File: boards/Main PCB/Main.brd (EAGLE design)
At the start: 101.6 x 76.2 mm, 89 parts, among them CN1 MINIB, CN2 MINIB, IC1 FT232RL, IC2 FT232RL, J1 3_PIN_JST-XH, J2 2_PIN_JST-XH, Q4 BSS138, Q5 BSS138, Q6 BSS138, Q7 BSS138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

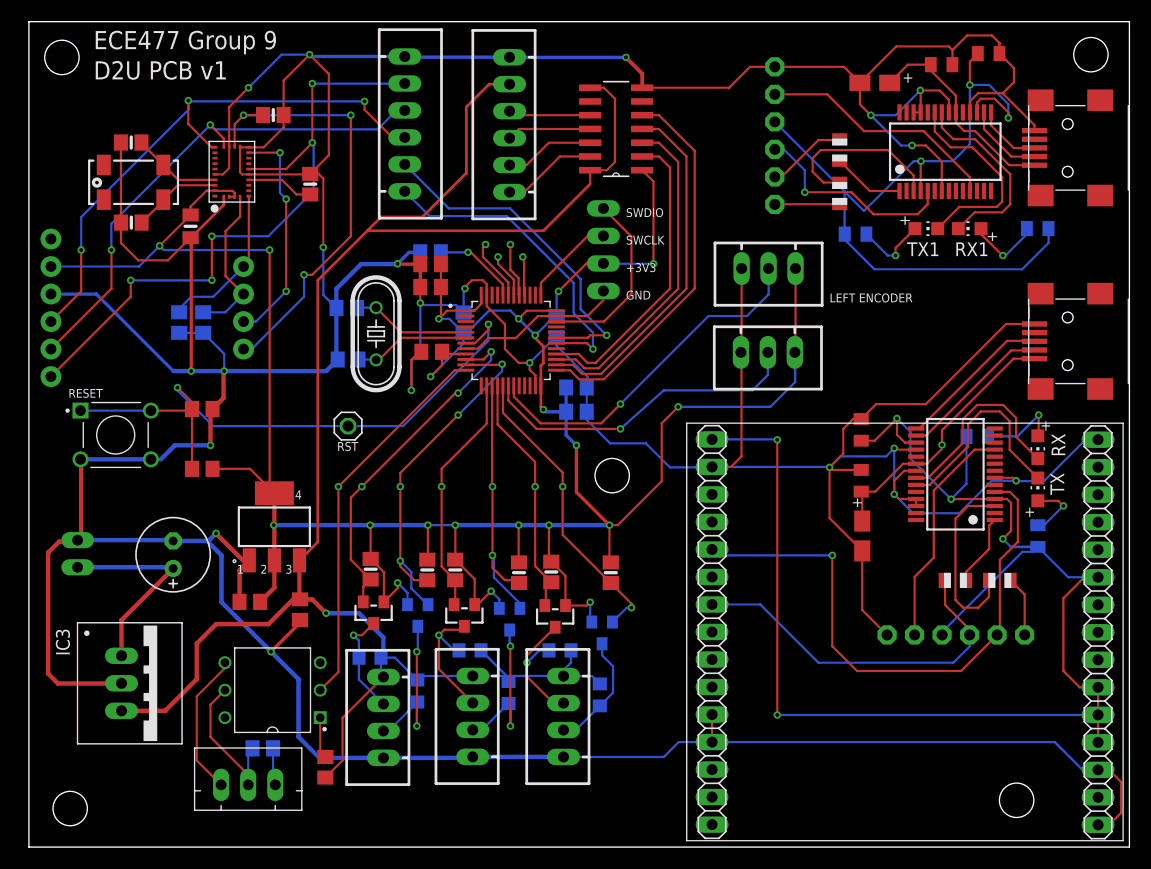
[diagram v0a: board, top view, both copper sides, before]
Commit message: Fixed minor routing problems
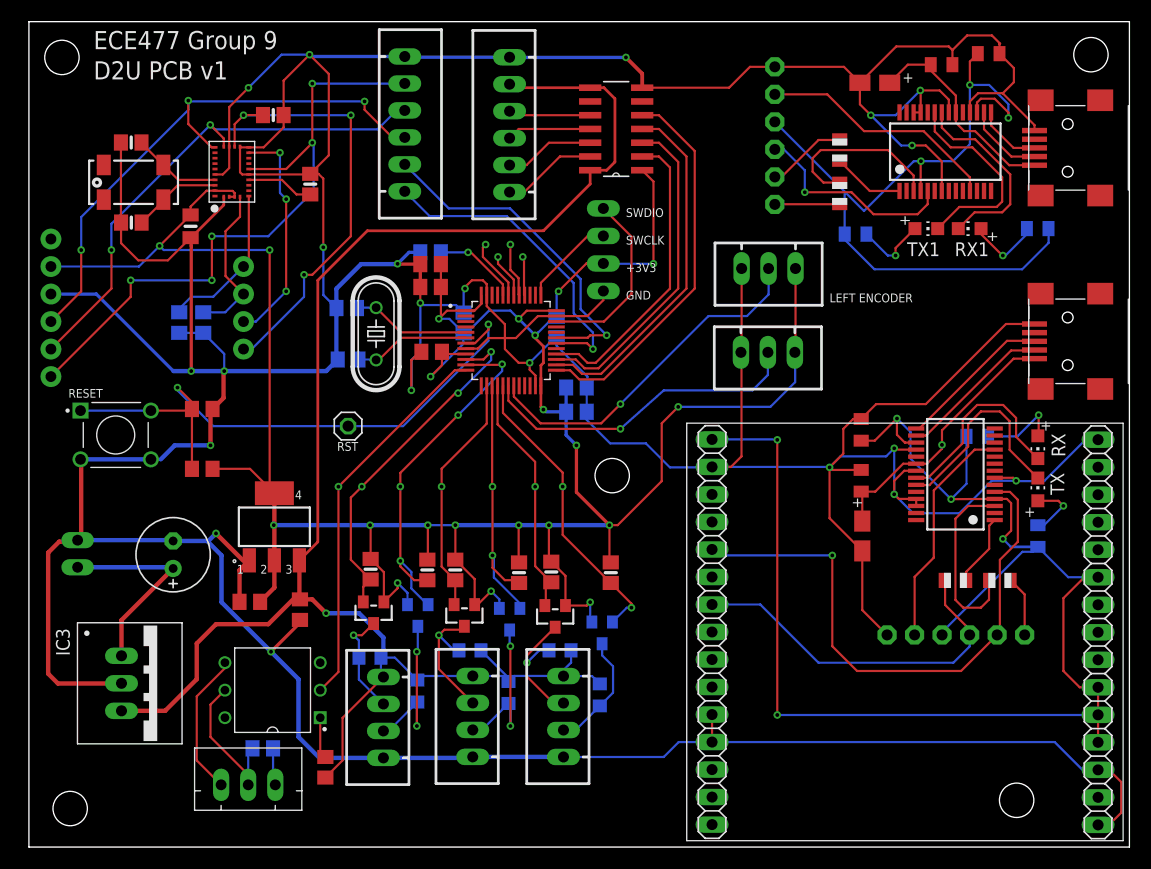
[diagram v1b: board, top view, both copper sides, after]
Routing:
- net +5V: track 169.6 -> 154.9 mm
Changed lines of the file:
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@@
 <?xml version="1.0" encoding="utf-8"?>
 <!DOCTYPE eagle SYSTEM "eagle.dtd">
-<eagle version="9.2.2">
+<eagle version="9.3.0">
 <drawing>
 <settings>
@@
 </element>
 <element name="C1" library="adafruit" package="A/3216-18R" value="10uF" x="76.936" y="28.716" smashed="yes" rot="R90">
-<attribute name="VALUE" x="79.261" y="26.766" size="0.6096" layer="27" rot="R90"/>
+<attribute name="VALUE" x="79.007" y="26.766" size="0.6096" layer="27" rot="R90"/>
 </element>
 <element name="C2" library="adafruit" package="C0805K" value="0.1uF" x="76.836" y="33.816" smashed="yes" rot="R90">
@@
 </element>
 <element name="R5" library="adafruit" package="R0805" value="10" x="85.536" y="24.616" smashed="yes">
-<attribute name="VALUE" x="84.774" y="22.33" size="0.6096" layer="27"/>
+<attribute name="VALUE" x="83.25" y="22.838" size="0.6096" layer="27"/>
 </element>
 <element name="FTDI" library="adafruit" package="1X06-CLEANBIG" value="" x="85.576" y="19.586" smashed="yes">
@@
 </element>
 <element name="R1" library="adafruit" package="R0805" value="10" x="89.636" y="24.616" smashed="yes" rot="R180">
-<attribute name="VALUE" x="90.398" y="26.902" size="0.6096" layer="27" rot="R180"/>
+<attribute name="VALUE" x="89.128" y="26.394" size="0.6096" layer="27" rot="R180"/>
 </element>
 <element name="U$3" library="microbuilder" package="BNO055" value="BNO055" x="18.74" y="62.346" smashed="yes" rot="R90">
@@
 <wire x1="26.67" y1="52.324" x2="31.242" y2="56.896" width="0.254" layer="1"/>
 <contactref element="X1" pad="5"/>
-<wire x1="31.242" y1="56.896" x2="32.512" y2="58.166" width="0.254" layer="1"/>
-<wire x1="32.512" y1="58.166" x2="36.322" y2="58.166" width="0.254" layer="1"/>
-<wire x1="36.322" y1="58.166" x2="40.386" y2="62.23" width="0.254" layer="1"/>
-<wire x1="40.386" y1="62.23" x2="40.386" y2="68.326" width="0.254" layer="1"/>
-<wire x1="40.386" y1="68.326" x2="42.4858" y2="70.4258" width="0.254" layer="1"/>
-<wire x1="42.4858" y1="70.4258" x2="44.374" y2="70.4258" width="0.254" layer="1"/>
 <contactref element="U4" pad="14"/>
 <contactref element="U4" pad="8"/>
-<wire x1="51.816" y1="70.104" x2="53.086" y2="70.104" width="0.2032" layer="1"/>
-<wire x1="53.086" y1="70.104" x2="54.102" y2="69.088" width="0.2032" layer="1"/>
-<wire x1="54.102" y1="69.088" x2="54.102" y2="63.246" width="0.2032" layer="1"/>
-<wire x1="54.102" y1="63.246" x2="53.34" y2="62.484" width="0.2032" layer="1"/>
-<wire x1="53.34" y1="62.484" x2="51.816" y2="62.484" width="0.2032" layer="1"/>
-<wire x1="51.816" y1="61.214" x2="51.816" y2="62.484" width="0.2032" layer="1"/>
+<wire x1="51.816" y1="70.104" x2="53.086" y2="70.104" width="0.254" layer="1"/>
+<wire x1="53.086" y1="70.104" x2="54.102" y2="69.088" width="0.254" layer="1"/>
+<wire x1="54.102" y1="69.088" x2="54.102" y2="63.246" width="0.254" layer="1"/>
+<wire x1="54.102" y1="63.246" x2="53.34" y2="62.484" width="0.254" layer="1"/>
+<wire x1="53.34" y1="62.484" x2="51.816" y2="62.484" width="0.254" layer="1"/>
+<wire x1="51.816" y1="61.214" x2="51.816" y2="62.484" width="0.254" layer="1"/>
+<wire x1="51.816" y1="70.104" x2="44.6958" y2="70.104" width="0.254" layer="1"/>
+<wire x1="44.6958" y1="70.104" x2="44.374" y2="70.4258" width="0.254" layer="1"/>
 </signal>
 <signal name="N$5">
@@
 <wire x1="85.536" y1="30.316" x2="85.536" y2="22.816" width="0.2032" layer="1"/>
 <wire x1="85.536" y1="22.816" x2="86.254" y2="22.098" width="0.2032" layer="1"/>
-<wire x1="86.254" y1="22.098" x2="87.63" y2="22.098" width="0.2032" layer="1"/>
-<wire x1="87.63" y1="22.098" x2="88.636" y2="23.104" width="0.2032" layer="1"/>
-<wire x1="88.636" y1="23.104" x2="88.636" y2="24.616" width="0.2032" layer="1"/>
+<wire x1="86.254" y1="22.098" x2="87.884" y2="22.098" width="0.2032" layer="1"/>
+<wire x1="87.884" y1="22.098" x2="88.636" y2="22.85" width="0.2032" layer="1"/>
+<wire x1="88.636" y1="22.85" x2="88.636" y2="24.616" width="0.2032" layer="1"/>
 <wire x1="86.711" y1="31.491" x2="85.536" y2="30.316" width="0.2032" layer="1"/>
 </signal>
@@
 <contactref element="Y1" pad="P$4"/>
 <wire x1="17.1775" y1="61.096" x2="13.737" y2="61.096" width="0.2032" layer="1"/>
-<wire x1="10.38" y1="57.679" x2="10.407" y2="57.652" width="0.2032" layer="1"/>
 <wire x1="13.737" y1="61.096" x2="12.412" y2="59.771" width="0.2032" layer="1"/>
 <wire x1="12.412" y1="59.771" x2="12.412" y2="59.657" width="0.2032" layer="1"/>

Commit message: More routing and naming improvements
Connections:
- net N$40 renamed SABERTOOTH_S1
- net N$41 renamed SABERTOOTH_5V
- net N$42 renamed SABERTOOTH_GND
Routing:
- net GND: track 648.5 -> 646.2 mm
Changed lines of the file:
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@@
 <drawing>
 <settings>
-<setting alwaysvectorfont="no"/>
+<setting alwaysvectorfont="yes"/>
 <setting verticaltext="up"/>
 </settings>
@@
 </layers>
 <board>
-<fusionsync huburn="a.cGVyc29uYWw6dWUyYTZiNjY2" projecturn="a.cGVyc29uYWw6dWUyYTZiNjY2I0QyMDE4MDEyNjExNDM0NjI1Ng" f3durn="urn:adsk.wipprod:dm.lineage:n0fbRr_KT-25qyjz7S21eg" pcbguid="6d30f37e-4e16-49f5-a01d-9dac6a8f2f00" lastpulledtime="" lastsyncedchangeguid="4fb3dc34-9c1d-74fe-b5d9-68b589e5fe3c"/>
+<fusionsync huburn="a.cGVyc29uYWw6dWUyYTZiNjY2" projecturn="a.cGVyc29uYWw6dWUyYTZiNjY2I0QyMDE4MDEyNjExNDM0NjI1Ng" f3durn="urn:adsk.wipprod:dm.lineage:n0fbRr_KT-25qyjz7S21eg" pcbguid="6d30f37e-4e16-49f5-a01d-9dac6a8f2f00" lastpulledtime="" lastsyncedchangeguid="b89508fb-dbec-dd2d-4bc5-ea25bebb0203"/>
 <plain>
 <wire x1="0" y1="0" x2="101.6" y2="0" width="0" layer="20"/>
@@
 <contactref element="U$1" pad="17"/>
 <contactref element="U$1" pad="26"/>
-<wire x1="63.0668" y1="12.2334" x2="63.0668" y2="9.6934" width="0.2032" layer="1"/>
+<wire x1="63.0668" y1="12.2334" x2="63.0668" y2="9.6934" width="0.4064" layer="1"/>
 <contactref element="CN2" pad="GND"/>
 <contactref element="IC2" pad="7"/>
@@
 <wire x1="2.794" y1="28.194" x2="1.778" y2="27.178" width="0.4064" layer="1"/>
 <wire x1="8.53" y1="15.1" x2="8.548" y2="15.118" width="0.2032" layer="1"/>
-<wire x1="13.314" y1="28.258" x2="16.574" y2="28.258" width="0.4064" layer="16"/>
-<wire x1="16.574" y1="28.258" x2="17.272" y2="28.956" width="0.4064" layer="16"/>
-<via x="17.272" y="28.956" extent="1-16" drill="0.35"/>
-<wire x1="16.574" y1="28.258" x2="16.574" y2="28.13" width="0.2032" layer="16"/>
-<wire x1="16.574" y1="28.13" x2="17.78" y2="26.924" width="0.4064" layer="16"/>
-<wire x1="17.78" y1="26.924" x2="17.78" y2="22.606" width="0.4064" layer="16"/>
-<wire x1="17.78" y1="22.606" x2="22.352" y2="18.034" width="0.4064" layer="16"/>
+<wire x1="16.32" y1="28.385" x2="13.441" y2="28.385" width="0.4064" layer="16"/>
+<wire x1="13.314" y1="28.258" x2="13.441" y2="28.385" width="0.4064" layer="16"/>
+<via x="17.78" y="26.924" extent="1-16" drill="0.35"/>
+<wire x1="22.352" y1="18.034" x2="17.78" y2="22.606" width="0.4064" layer="16"/>
 <via x="22.352" y="18.034" extent="1-16" drill="0.35"/>
 <wire x1="22.352" y1="18.034" x2="25.022" y2="20.704" width="0.3048" layer="1"/>
@@
 <wire x1="39.433" y1="50.038" x2="36.322" y2="50.038" width="0.2032" layer="16"/>
 <wire x1="42.264" y1="50.948" x2="42.264" y2="49.938" width="0.2032" layer="1"/>
-<wire x1="49.352" y1="8.3162" x2="58.6082" y2="8.3162" width="0.2032" layer="16"/>
-<wire x1="59.9854" y1="9.6934" x2="63.0668" y2="9.6934" width="0.2032" layer="16"/>
-<wire x1="58.6082" y1="8.3162" x2="59.9854" y2="9.6934" width="0.2032" layer="16"/>
-<wire x1="63.0668" y1="9.6934" x2="94.7006" y2="9.6934" width="0.2032" layer="16"/>
-<wire x1="97.266" y1="7.128" x2="98.703" y2="7.128" width="0.2032" layer="16"/>
-<wire x1="94.7006" y1="9.6934" x2="97.266" y2="7.128" width="0.2032" layer="16"/>
+<wire x1="49.352" y1="8.3162" x2="58.6082" y2="8.3162" width="0.4064" layer="16"/>
+<wire x1="59.9854" y1="9.6934" x2="63.0668" y2="9.6934" width="0.4064" layer="16"/>
+<wire x1="58.6082" y1="8.3162" x2="59.9854" y2="9.6934" width="0.4064" layer="16"/>
+<wire x1="63.0668" y1="9.6934" x2="94.7006" y2="9.6934" width="0.4064" layer="16"/>
+<wire x1="97.266" y1="7.128" x2="98.703" y2="7.128" width="0.4064" layer="16"/>
+<wire x1="94.7006" y1="9.6934" x2="97.266" y2="7.128" width="0.4064" layer="16"/>
 <via x="40.259" y="51.562" extent="1-16" drill="0.35"/>
 <wire x1="42.264" y1="50.948" x2="42.264" y2="51.97" width="0.2032" layer="1"/>
@@
 <wire x1="82.296" y1="69.85" x2="80.01" y2="67.564" width="0.2032" layer="16"/>
 <wire x1="80.01" y1="67.564" x2="77.724" y2="67.564" width="0.2032" layer="16"/>
-<wire x1="100.838" y1="6.009" x2="100.838" y2="3.167" width="0.2032" layer="1"/>
-<wire x1="100.838" y1="3.167" x2="99.719" y2="2.048" width="0.2032" layer="1"/>
+<wire x1="100.838" y1="6.009" x2="100.838" y2="3.167" width="0.4064" layer="1"/>
+<wire x1="100.838" y1="3.167" x2="99.719" y2="2.048" width="0.4064" layer="1"/>
 <wire x1="98.703" y1="2.048" x2="99.719" y2="2.048" width="0.2032" layer="1"/>
-<wire x1="100.838" y1="6.009" x2="99.719" y2="7.128" width="0.2032" layer="1"/>
+<wire x1="100.838" y1="6.009" x2="99.719" y2="7.128" width="0.4064" layer="1"/>
 <wire x1="98.703" y1="7.128" x2="99.719" y2="7.128" width="0.2032" layer="1"/>
 <wire x1="98.703" y1="37.608" x2="97.552" y2="37.608" width="0.2032" layer="16"/>
@@
 <wire x1="40.974" y1="8.3262" x2="49.342" y2="8.3262" width="0.4064" layer="16"/>
 <wire x1="49.342" y1="8.3262" x2="49.352" y2="8.3162" width="0.2032" layer="16"/>
-<wire x1="19.7997" y1="26.4283" x2="20.3077" y2="26.4283" width="0.2032" layer="1"/>
-<wire x1="17.272" y1="28.956" x2="19.7997" y2="26.4283" width="0.4064" layer="1"/>
+<wire x1="18.2757" y1="26.4283" x2="20.3077" y2="26.4283" width="0.4064" layer="1"/>
+<wire x1="17.78" y1="26.924" x2="18.2757" y2="26.4283" width="0.4064" layer="1"/>
 <wire x1="34.698" y1="72.983" x2="26.077" y2="72.983" width="0.3048" layer="16"/>
 <wire x1="26.077" y1="72.983" x2="25.908" y2="73.152" width="0.3048" layer="16"/>
@@
 <wire x1="12.8315" y1="54.1655" x2="14.924" y2="56.258" width="0.2032" layer="1"/>
 <wire x1="10.0965" y1="54.1655" x2="12.8315" y2="54.1655" width="0.2032" layer="1"/>
+<wire x1="17.78" y1="22.606" x2="17.78" y2="26.924" width="0.4064" layer="16"/>
+<wire x1="17.78" y1="26.924" x2="17.78" y2="26.925" width="0.4064" layer="16"/>
+<wire x1="17.78" y1="26.925" x2="16.32" y2="28.385" width="0.4064" layer="16"/>
 </signal>
 <signal name="D+_GPS">
@@
 <wire x1="52.07" y1="47.498" x2="50.292" y2="49.276" width="0.2032" layer="16"/>
 <wire x1="50.292" y1="49.276" x2="50.292" y2="52.07" width="0.2032" layer="16"/>
-<wire x1="50.292" y1="52.07" x2="44.111" y2="58.251" width="0.2032" layer="16"/>
-<wire x1="44.111" y1="58.251" x2="36.984" y2="58.251" width="0.2032" layer="16"/>
-<wire x1="36.984" y1="58.251" x2="34.698" y2="60.537" width="0.2032" layer="16"/>
+<wire x1="50.292" y1="52.07" x2="45.127" y2="57.235" width="0.2032" layer="16"/>
+<wire x1="45.127" y1="57.235" x2="38" y2="57.235" width="0.2032" layer="16"/>
+<wire x1="38" y1="57.235" x2="34.698" y2="60.537" width="0.2032" layer="16"/>
 </signal>
 <signal name="N$39">
@@
 <wire x1="53.34" y1="47.244" x2="50.927" y2="49.657" width="0.2032" layer="16"/>
 <wire x1="50.927" y1="49.657" x2="50.927" y2="52.451" width="0.2032" layer="16"/>
-<wire x1="50.927" y1="52.451" x2="44.4158" y2="58.9622" width="0.2032" layer="16"/>
-<wire x1="44.4158" y1="58.9622" x2="38.762" y2="58.9622" width="0.2032" layer="16"/>
-<wire x1="38.762" y1="58.9622" x2="34.698" y2="63.0262" width="0.2032" layer="16"/>
-</signal>
-<signal name="N$40">
+<wire x1="50.927" y1="52.451" x2="45.1778" y2="58.2002" width="0.2032" layer="16"/>
+<wire x1="45.1778" y1="58.2002" x2="39.524" y2="58.2002" width="0.2032" layer="16"/>
+<wire x1="39.524" y1="58.2002" x2="34.698" y2="63.0262" width="0.2032" layer="16"/>
+</signal>
+<signal name="SABERTOOTH_S1">
 <contactref element="J1" pad="P$1"/>
 <contactref element="R20" pad="2"/>
@@
 <wire x1="22.54" y1="5.95" x2="22.744" y2="5.746" width="0.2032" layer="16"/>
 </signal>
-<signal name="N$41">
+<signal name="SABERTOOTH_5V">
 <contactref element="R20" pad="1"/>
 <contactref element="U3" pad="5"/>
@@
 <wire x1="20.244" y1="8.72" x2="20.244" y2="5.746" width="0.2032" layer="16"/>
 </signal>
-<signal name="N$42">
+<signal name="SABERTOOTH_GND">
 <contactref element="J1" pad="P$3"/>
 <contactref element="U3" pad="4"/>

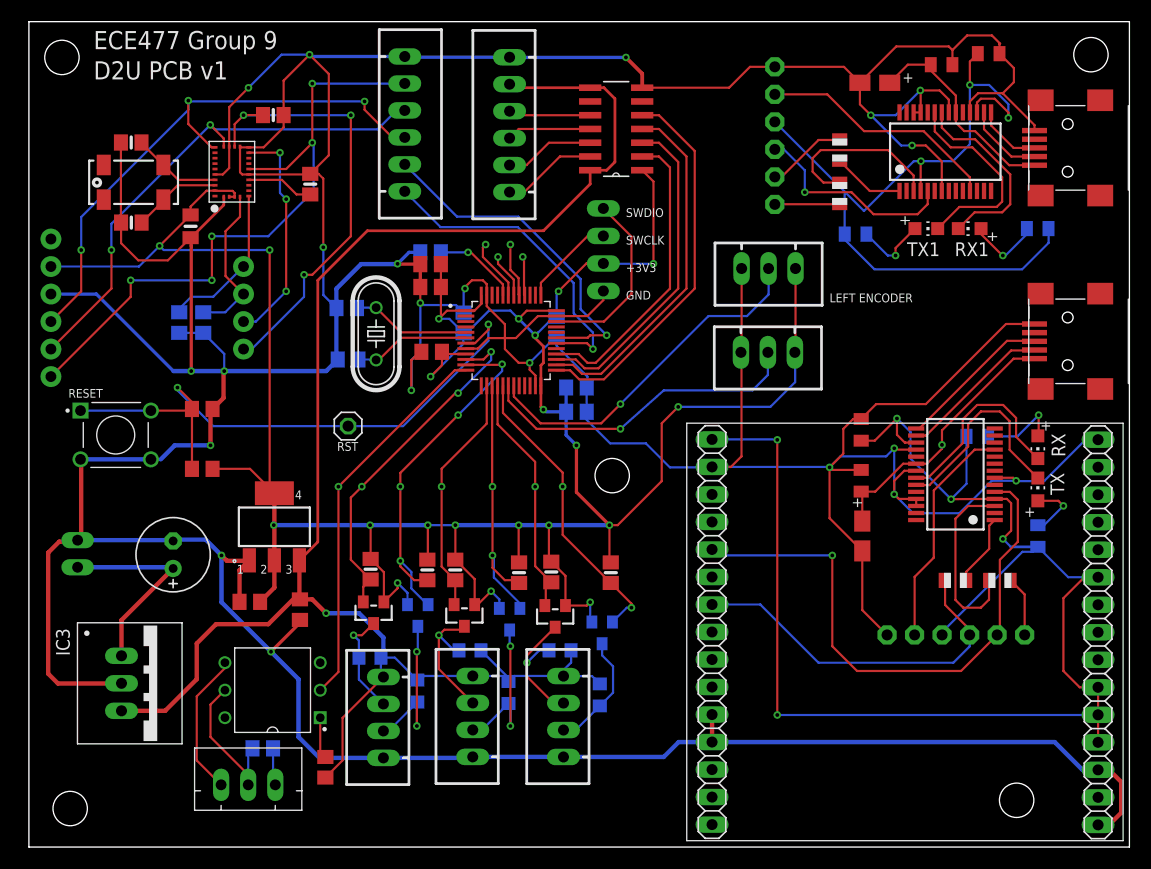
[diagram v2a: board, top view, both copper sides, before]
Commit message: Minor routing improvements and net naming
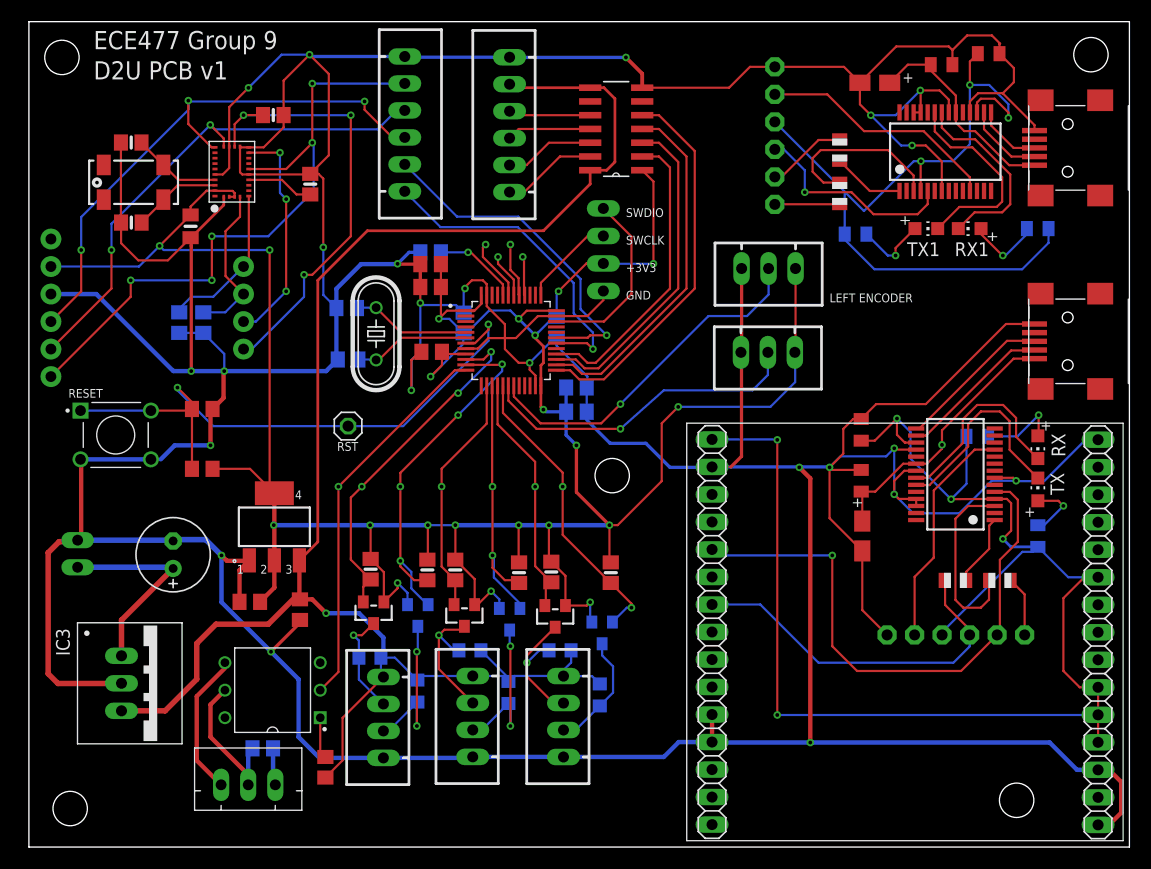
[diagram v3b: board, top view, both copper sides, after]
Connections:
- net SABERTOOTH_5V: now also J1.P$1, R20.2; no longer J1.P$2, R20.1, U3.5
- net SABERTOOTH_S1: now also J1.P$2, R20.1, U3.5; no longer J1.P$1, R20.2
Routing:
- net GND: track 646.2 -> 672.1 mm, vias 21 -> 23
- net SABERTOOTH_S1: track 3.45 -> 14.3 mm
- net SABERTOOTH_5V: track 14.3 -> 3.45 mm
